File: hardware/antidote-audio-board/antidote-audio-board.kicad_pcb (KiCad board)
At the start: 4 copper layers, 65 x 30 mm, 60 parts, among them J1 Cubie GPIO, J2 Instrument Out, J3 Phones, J4 Instrument In, J5 LED Header, J6 I2C Header, SW1 Footswitch, SW2 Footswitch, U1 ADS1115IDGS, U2 MCP6002-xSN, U3 TAC5112IRGER, U4 LP5907MFX-3.3

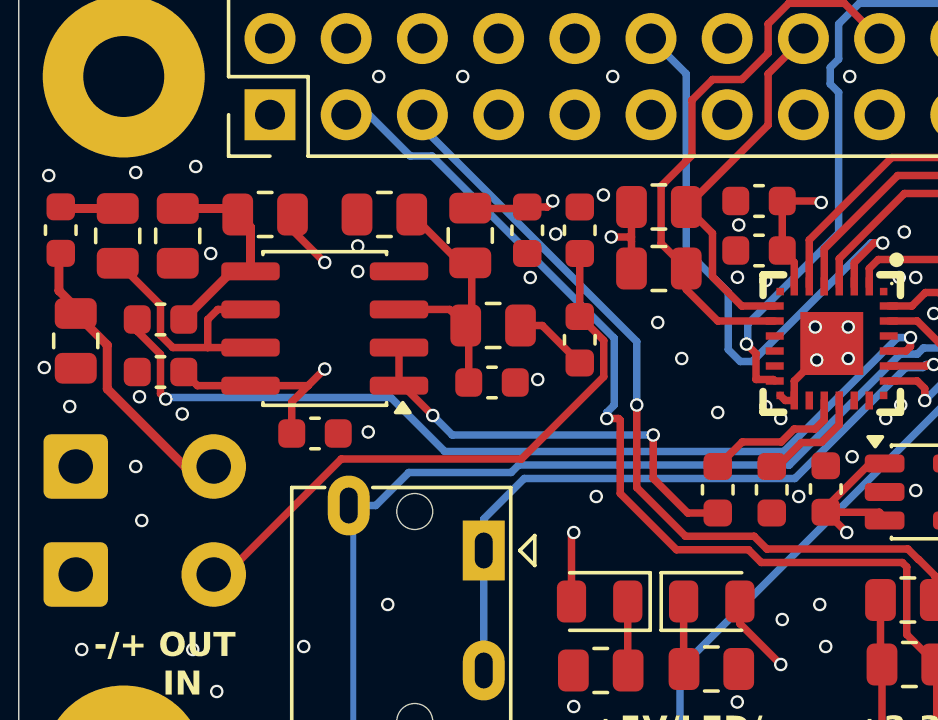
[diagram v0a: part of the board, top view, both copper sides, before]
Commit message: feat: add rc tap to clean op-amp noise
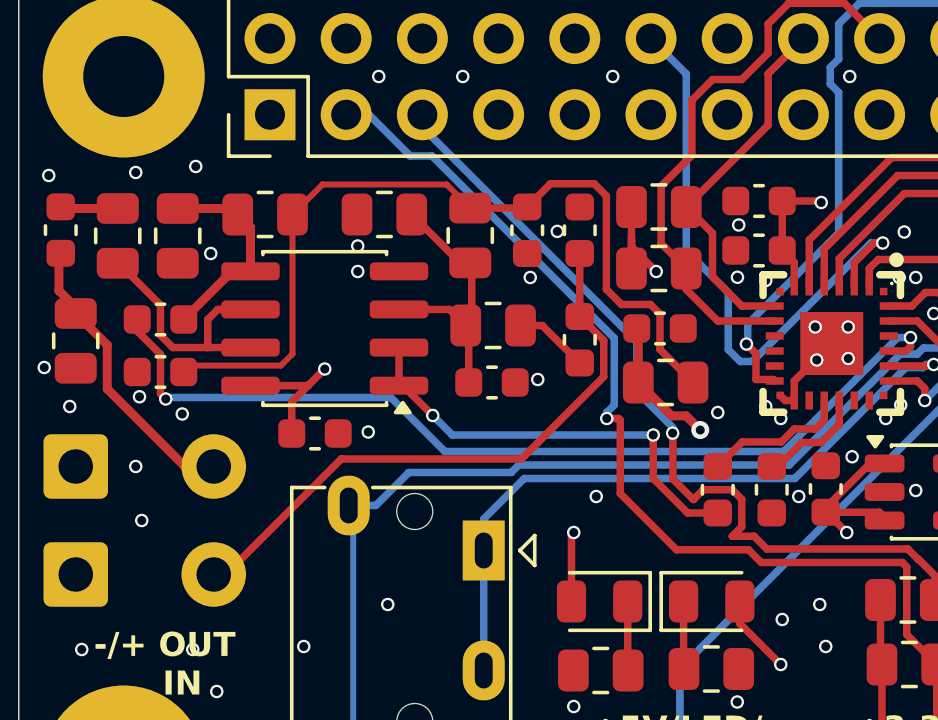
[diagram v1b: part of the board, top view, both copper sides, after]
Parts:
- added C21: 10 uF, Capacitor_SMD:C_0603_1608Metric, F.Cu at (53.9, 44.4)
- added R16: 10 K, Resistor_SMD:R_0805_2012Metric, F.Cu at (54.1, 46.2)
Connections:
- C13 pad 1: +5V -> +5V Filtered
- C4 pad 1: +5V -> +5V Filtered
- R2 pad 1: +5V -> +5V Filtered
- R7 pad 1: +5V -> +5V Filtered
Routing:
- net +5V Filtered: track 0.00 -> 28.3 mm
- net +5V: track 73.1 -> 69.4 mm, vias 5 -> 4
- net +3V3: track 136.1 -> 137.6 mm
- net /SCK I2C0: track 35.8 -> 36.4 mm
- net GND: vias 131 -> 128
